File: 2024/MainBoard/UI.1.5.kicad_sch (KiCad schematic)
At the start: 54 parts, among them J1 Raspberry_Pi_2_3, J2 fan, J3 Debug, J4 USB_C_Receptacle_USB2.0_16P, J5 Can_debug, Q1 NMOS, SW1 SW_Coded_SH-7050, SW2 Ras_1, SW3 Ras_2, SW4 NRST, SW5 Boot, U1 MOUDLE-SEEEDUINO-XIAO, U2 MCP2562-E-P, U3 CH340E, U4 STM32F446RETx

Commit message: アートワークした
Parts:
- removed LED_Ras1, LED_main: R, Resistor_SMD:R_0402_1005Metric, symbol Device:R
- removed TFT3: ~, Connector_PinHeader_2.54mm:PinHeader_1x04_P2.54mm_Vertical, symbol Connector_Generic:Conn_01x04
- added R15, R8: R, Resistor_SMD:R_0402_1005Metric, symbol Device:R
- Connector_Sub1: footprint Connector_PinSocket_2.54mm:PinSocket_1x06_P2.54mm_Vertical -> Connector_JST:JST_XH_S6B-XH-A_1x06_P2.50mm_Horizontal
- D1: value LED -> LED_main
- D5: value LED -> LED_Ras1
- J1: footprint Connector_PinHeader_2.54mm:PinHeader_2x20_P2.54mm_Vertical -> Connector_PinSocket_2.54mm:PinSocket_2x20_P2.54mm_Vertical
- R2: value 600R -> 300
- SW4: footprint (none) -> Button_Switch_SMD:SW_SPST_Omron_B3FS-100xP
- TFT1: footprint Connector_PinHeader_2.54mm:PinHeader_1x08_P2.54mm_Vertical -> Connector_PinSocket_2.54mm:PinSocket_1x08_P2.54mm_Vertical
- TFT2: footprint Connector_PinHeader_2.54mm:PinHeader_1x04_P2.54mm_Vertical -> Connector_PinSocket_2.54mm:PinSocket_1x04_P2.54mm_Vertical
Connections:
- net GND: now also D1.1 (K), R15.2
- net Main_LED: now also R8.1; no longer D1.2 (A)
- net at D5.1 (K): now also R15.1
- new net: D1.2 (A), R8.2
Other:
- moved on the sheet: D1

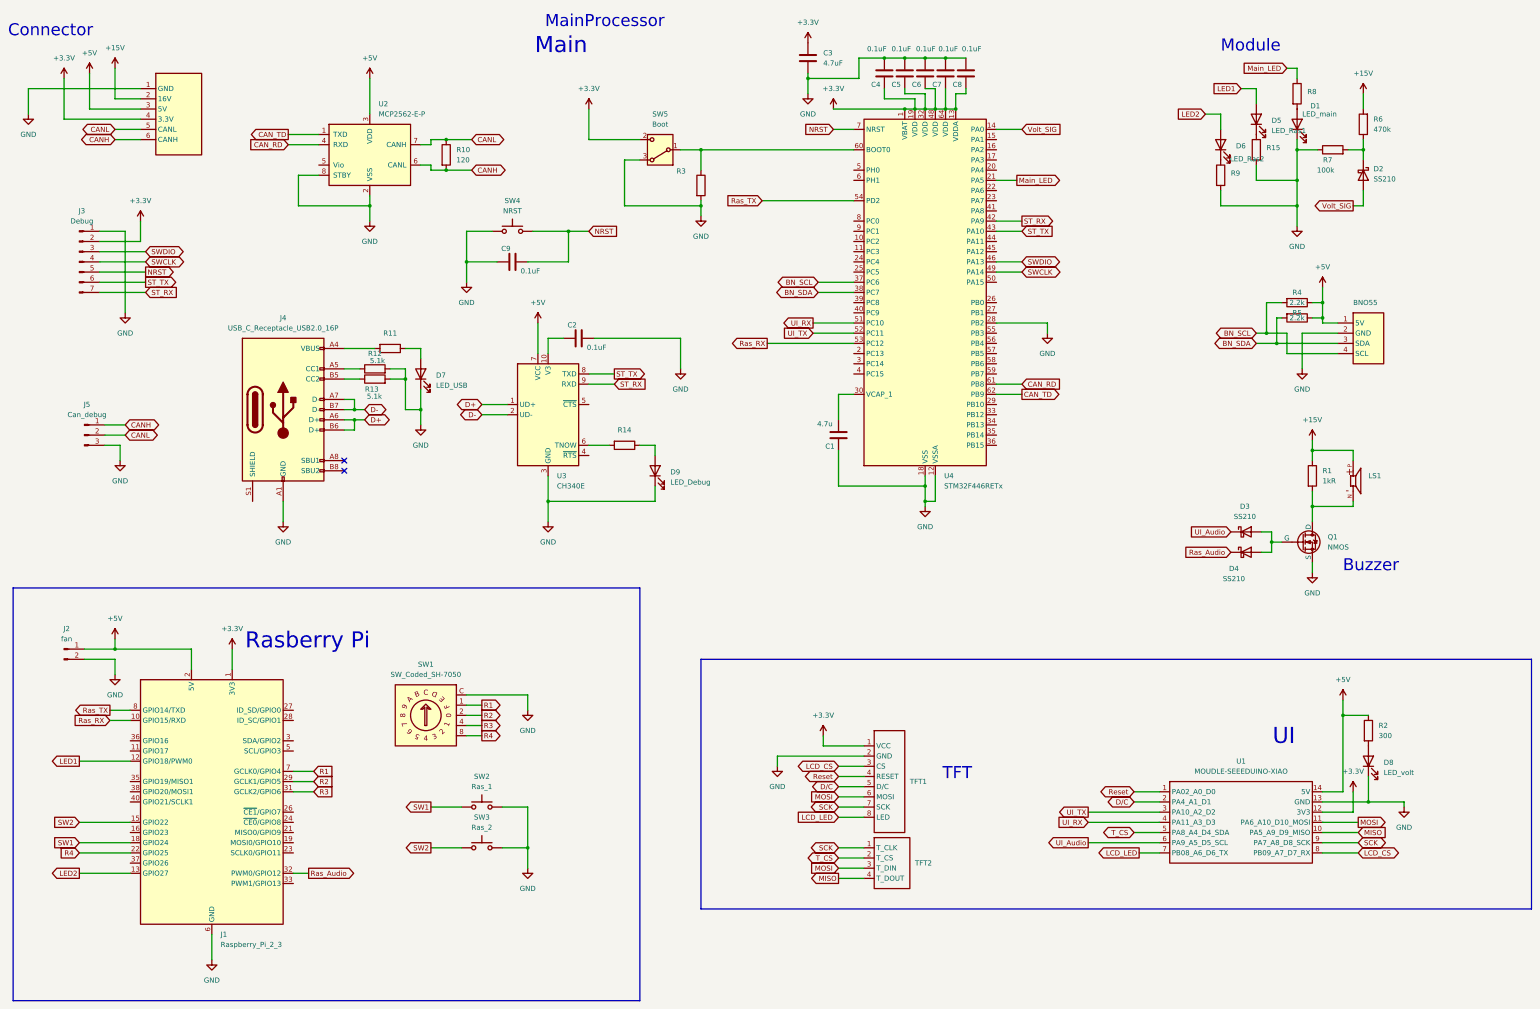
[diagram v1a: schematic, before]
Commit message: 最終版
未実装：canでの通信(mainとxiao）
dc-dc
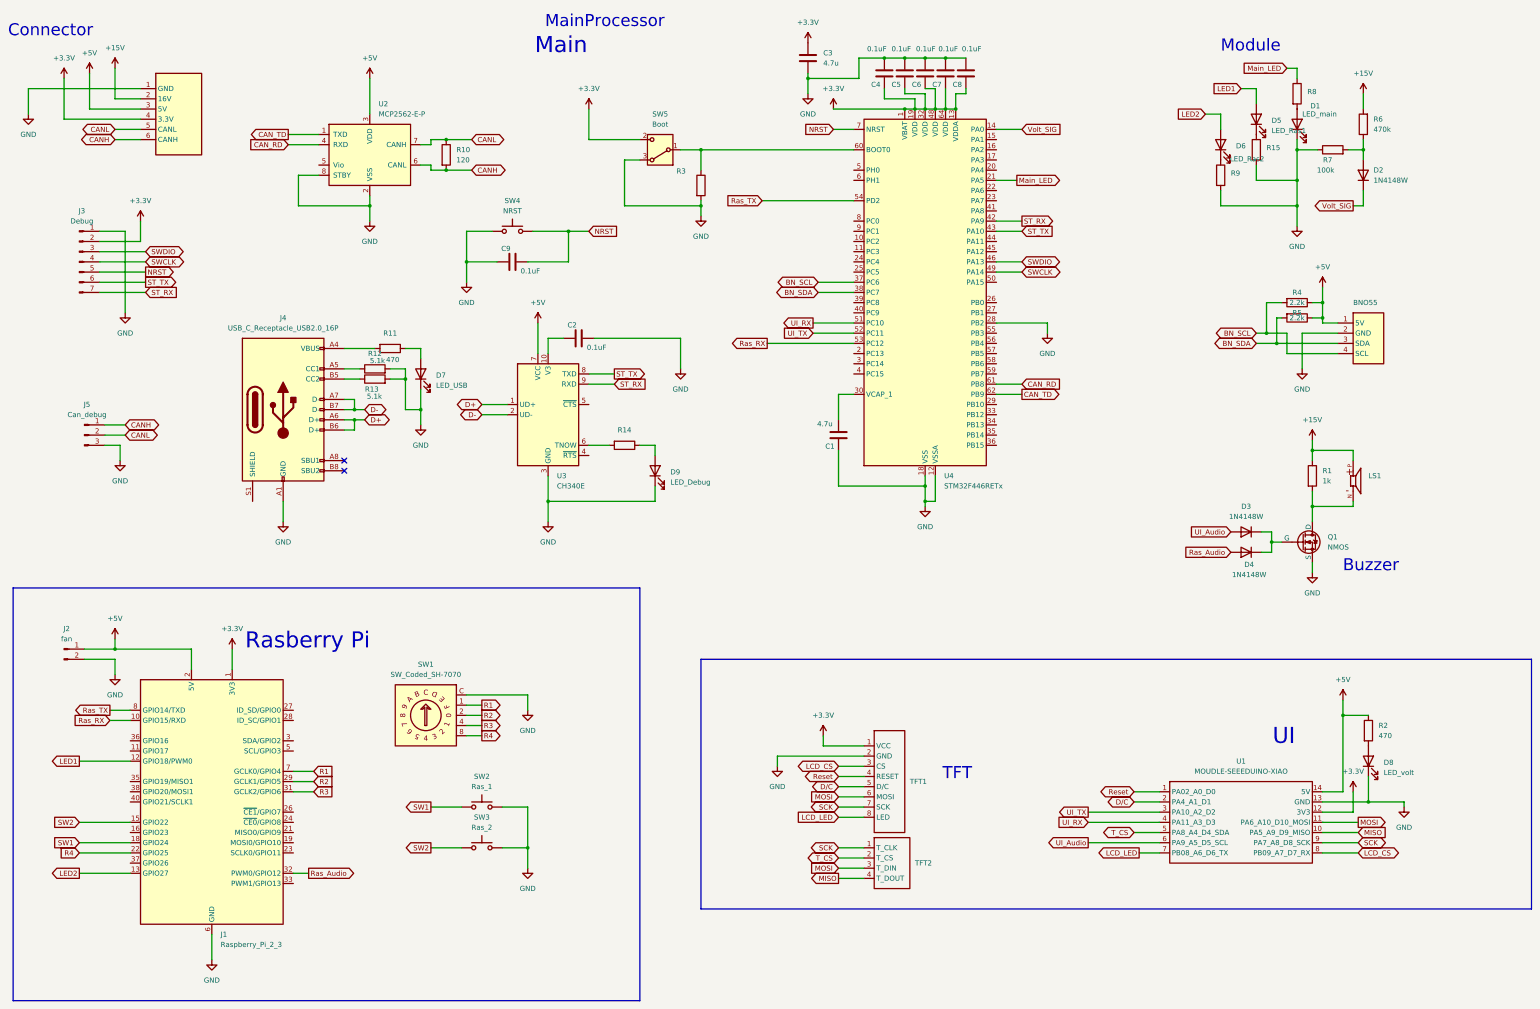
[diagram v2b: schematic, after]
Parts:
- removed D2, D3, D4: SS210, Diode_SMD:D_SMA, symbol Diode:SS210
- removed SW1: SW_Coded_SH-7050, Button_Switch_SMD:Nidec_Copal_SH-7010A, symbol Switch:SW_Coded_SH-7050
- added D2, D3, D4: 1N4148W, Diode_SMD:D_SOD-123, symbol Diode:1N4148W
- added SW1: SW_Coded_SH-7070, Button_Switch_THT:Nidec_Copal_SH-7010C, symbol Switch:SW_Coded_SH-7070
- C1, C2, C4, C5, C6, C7, C8, C9: footprint Capacitor_SMD:C_0402_1005Metric -> Capacitor_SMD:C_0603_1608Metric_Pad1.08x0.95mm_HandSolder
- C3: value 4.7uF -> 4.7u; footprint Capacitor_SMD:C_0402_1005Metric -> Capacitor_SMD:C_0603_1608Metric_Pad1.08x0.95mm_HandSolder
- R1: value 1kR -> 1k; footprint Resistor_SMD:R_0402_1005Metric -> Resistor_SMD:R_0603_1608Metric_Pad0.98x0.95mm_HandSolder
- R10, R12, R13, R4, R5, R6, R7: footprint Resistor_SMD:R_0402_1005Metric -> Resistor_SMD:R_0603_1608Metric_Pad0.98x0.95mm_HandSolder
- R11, R14: value 120 -> 470; footprint Resistor_SMD:R_0402_1005Metric -> Resistor_SMD:R_0603_1608Metric_Pad0.98x0.95mm_HandSolder
- R15, R8, R9: value R -> 300; footprint Resistor_SMD:R_0402_1005Metric -> Resistor_SMD:R_0603_1608Metric_Pad0.98x0.95mm_HandSolder
- R2: value 300 -> 470; footprint Resistor_SMD:R_0402_1005Metric -> Resistor_SMD:R_0603_1608Metric_Pad0.98x0.95mm_HandSolder
- R3: value 120 -> 300; footprint Resistor_SMD:R_0402_1005Metric -> Resistor_SMD:R_0603_1608Metric_Pad0.98x0.95mm_HandSolder
- SW2, SW3, SW4: footprint Button_Switch_SMD:SW_SPST_Omron_B3FS-100xP -> Button_Switch_THT:SW_PUSH_6mm_H7.3mm
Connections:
- net GND: now also SW1.C
- net R1: now also SW1.1
- net R2: now also SW1.2
- net R3: now also SW1.4
- net R4: now also SW1.8
- net Ras_Audio: now also D4.2 (A)
- net UI_Audio: now also D3.2 (A)
- net Volt_SIG: now also D2.1 (K)
- net at R6.1, R7.2: now also D2.2 (A)
- net at Q1.2 (G): now also D3.1 (K), D4.1 (K)

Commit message: 発注版
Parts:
- added C10, C11, C14, C15, C16: 0.1u, Capacitor_SMD:C_0603_1608Metric_Pad1.08x0.95mm_HandSolder, symbol Device:C
- added C12, C13: 0.1uF, Capacitor_SMD:C_0603_1608Metric_Pad1.08x0.95mm_HandSolder, symbol Device:C
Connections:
- net +3.3V: now also C11.1, C16.1
- net +5V: now also C10.1, C12.2, C13.2, C14.1, C15.1
- net GND: now also C10.2, C11.2, C12.1, C13.1, C14.2, C15.2, C16.2
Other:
- moved on the sheet: D8, J2, R2
